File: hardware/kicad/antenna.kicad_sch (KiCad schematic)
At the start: 12 parts, among them U13 MM8130-2600, U14 MM8130-2600, U15 SKY13414-485LF, U16 SKY13414-485LF, U17 MM8130-2600, U18 MM8130-2600

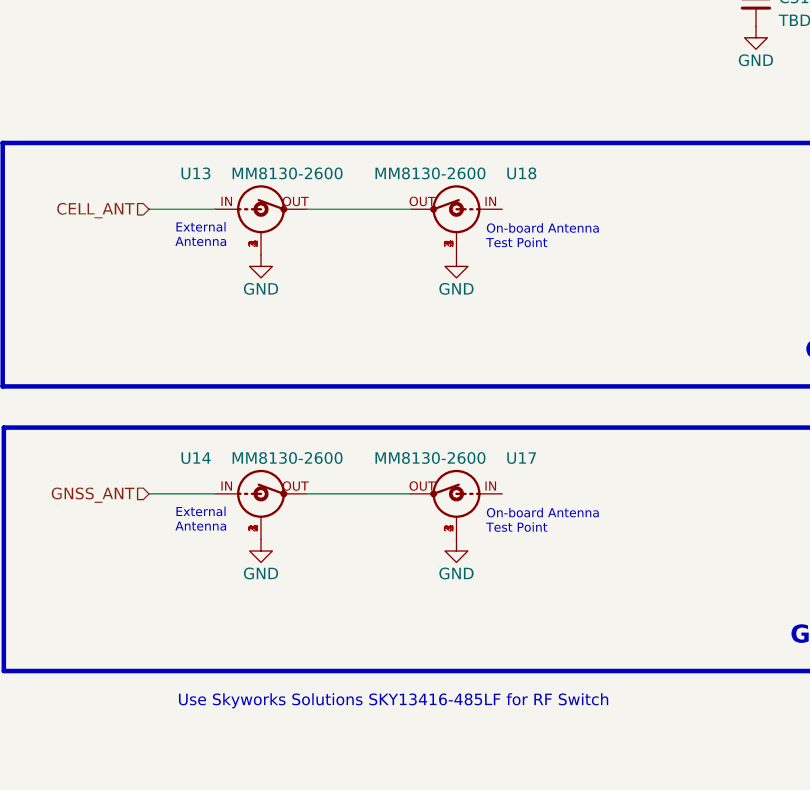
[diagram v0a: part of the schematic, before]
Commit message: remove antenna switch
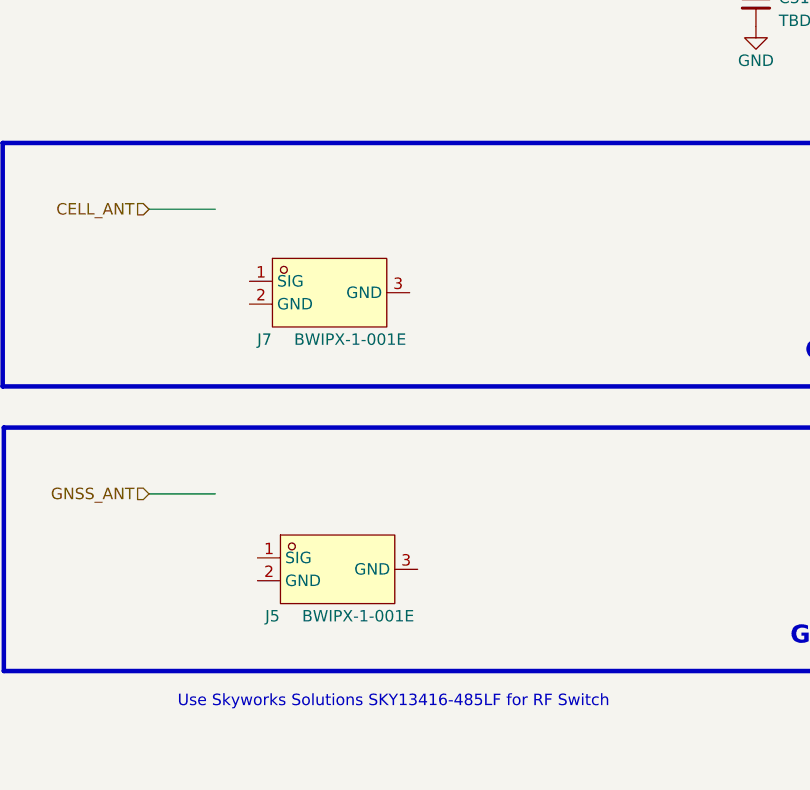
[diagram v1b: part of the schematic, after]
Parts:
- removed U13, U14, U17, U18: MM8130-2600, bwlc1a:MM8130-2600, symbol bwlc1a:MM8130-2600
- added J5, J7: BWIPX-1-001E, bwlc1a:BWIPX-1-001E, symbol bwlc1a:BWIPX-1-001E
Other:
- note removed: "External Antenna"
- note removed: "On-board Antenna Test Point"

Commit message: update antenna
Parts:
- added R20 (x2): 0, Resistor_SMD:R_0402_1005Metric, symbol Device:R_Small
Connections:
- net CELL_ANT: now also R20.1
- net GND: now also U15.15 (GND), U16.15 (GND)
- net at R20.1: now also U16.13 (ANT)
- net at J7.1 (SIG): now also R20.1, R20.2
- net at E1.1: now also R21.2
- net CELL_ANT_OUT: now reaches U15.13 (ANT)
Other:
- moved on the sheet: C31, C32, E1, J5, J7, R20, R21, U15, U16

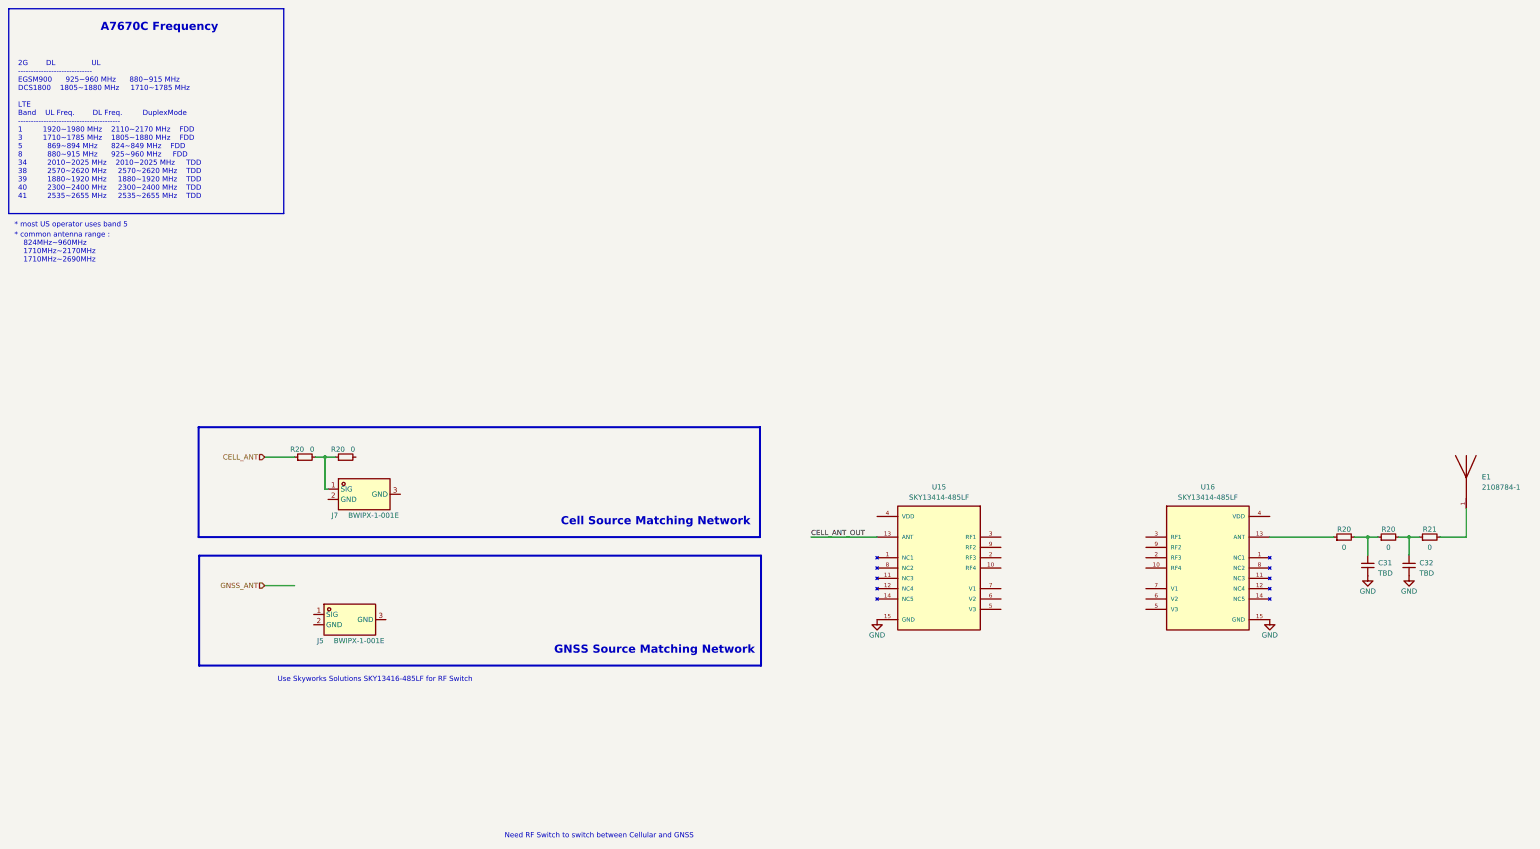
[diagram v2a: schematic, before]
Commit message: add te connectivity antenna schematicY
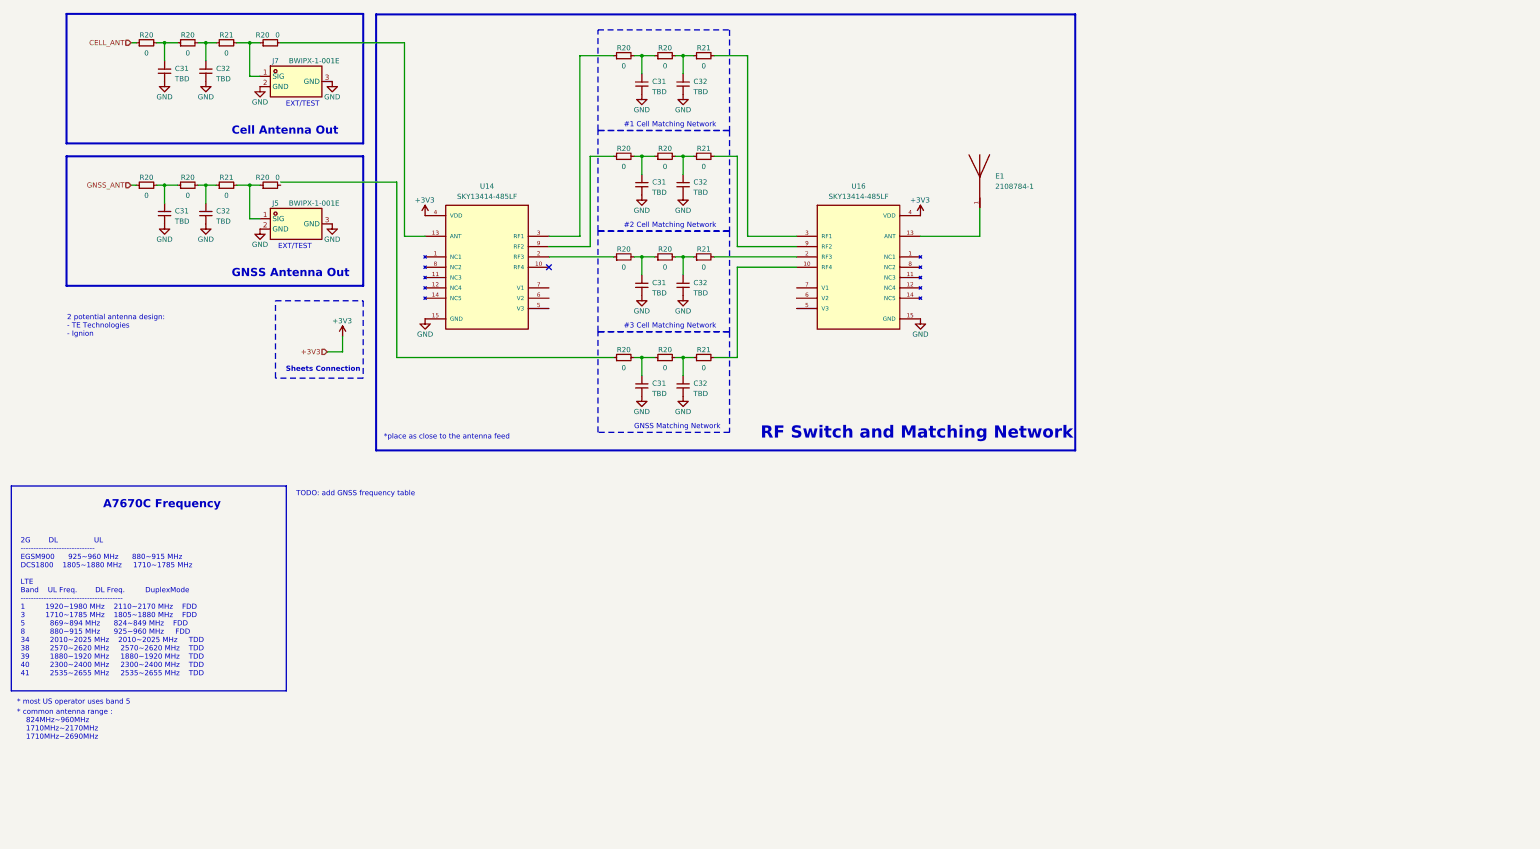
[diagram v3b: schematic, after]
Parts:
- removed C31, C32: TBD, Capacitor_SMD:C_0402_1005Metric, symbol Device:C_Small
- removed R20 (x4), R21: 0, Resistor_SMD:R_0402_1005Metric, symbol Device:R_Small
- removed U15: SKY13414-485LF, symbol bwlc1a:SKY13414-485LF
- added C31 (x6), C32 (x6): TBD, Capacitor_SMD:C_0402_1005Metric, symbol Device:C_Small
- added R20 (x14), R21 (x6): 0, Resistor_SMD:R_0402_1005Metric, symbol Device:R_Small
- added U14: SKY13414-485LF, symbol bwlc1a:SKY13414-485LF
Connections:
- net CELL_ANT: now also R20.1
- net GND: now also J5.2 (GND), J5.3 (GND), J7.2 (GND), J7.3 (GND), C31.2, C31.2, C31.2, C31.2, C31.2, C31.2, C32.2, C32.2, C32.2, C32.2, C32.2, C32.2, U14.15 (GND)
- net GNSS_ANT: now also R20.1
- net at U16.13 (ANT): now also E1.1
- net at J7.1 (SIG): now also R20.1, R21.2
- net at U16.10 (RF4): now also R21.2
- net at U16.2 (RF3): now also R21.2
- net at U16.3 (RF1): now also R21.2
- net +3V3: now reaches U16.4 (VDD)
- net +3V3: now also U14.4 (VDD)
- net at U16.9 (RF2): now also R21.2
- net at J5.1 (SIG): now also R20.1, R21.2
- new net: C32.1, R20.2, R21.1 (x6)
- new net: R20.2, U14.13 (ANT)
- new net: C31.1, R20.1, R20.2 (x6)
- new net: R20.1, U14.2 (RF3)
- new net: R20.1, U14.9 (RF2)
- new net: R20.1, U14.3 (RF1)
- no-connect marks 0 -> 1
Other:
- note added: "#1 Cell Matching Network"
- note added: "#2 Cell Matching Network"
- note added: "#3 Cell Matching Network"
- note added: "*place as close to the antenna feed"
- note added: "2 potential antenna design: - TE Technologies - Ignion"
- note added: "Cell Antenna Out"
- note added: "EXT/TEST"
- note added: "GNSS Antenna Out"
- note added: "GNSS Matching Network"
- note added: "RF Switch and Matching Network"
- note added: "Sheets Connection"
- note added: "TODO: add GNSS frequency table"
- note removed: "Cell Source Matching Network"
- note removed: "GNSS Source Matching Network"
- note removed: "Need RF Switch to switch between Cellular and GNSS"
- note removed: "Use Skyworks Solutions SKY13416-485LF for RF Switch"
- moved on the sheet: E1, U16

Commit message: add todo comment
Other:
- note added: "TODO: check design guide for rf switch"
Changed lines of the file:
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@@
+    (effects (font (size 1.27 1.27)) (justify left bottom))
+  )
+  (text "TODO: check design guide for rf switch" (at 114.3 53.975 0)
     (effects (font (size 1.27 1.27)) (justify left bottom))
   )

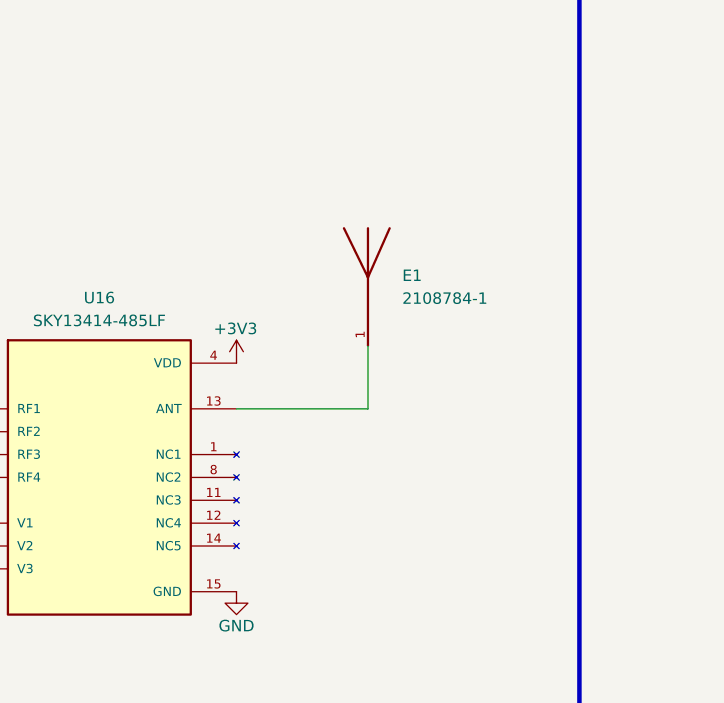
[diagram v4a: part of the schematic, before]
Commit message: add matching network close to antenna feed
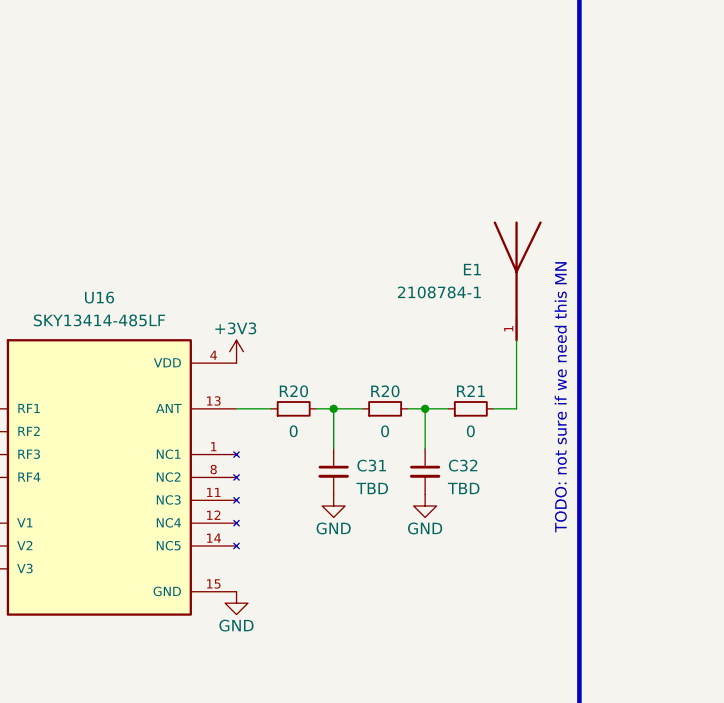
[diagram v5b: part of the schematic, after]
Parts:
- added C31, C32: TBD, Capacitor_SMD:C_0402_1005Metric, symbol Device:C_Small
- added R20 (x2), R21: 0, Resistor_SMD:R_0402_1005Metric, symbol Device:R_Small
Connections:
- net GND: now also C31.2, C32.2
- net at E1.1: now also R21.2; no longer U16.13 (ANT)
- new net: C31.1, R20.1, R20.2
- new net: C32.1, R20.2, R21.1
- new net: R20.1, U16.13 (ANT)
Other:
- note added: "TODO: not sure if we need this MN"
- moved on the sheet: E1

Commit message: clean-up
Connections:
- net at R20.2: now also R20.1

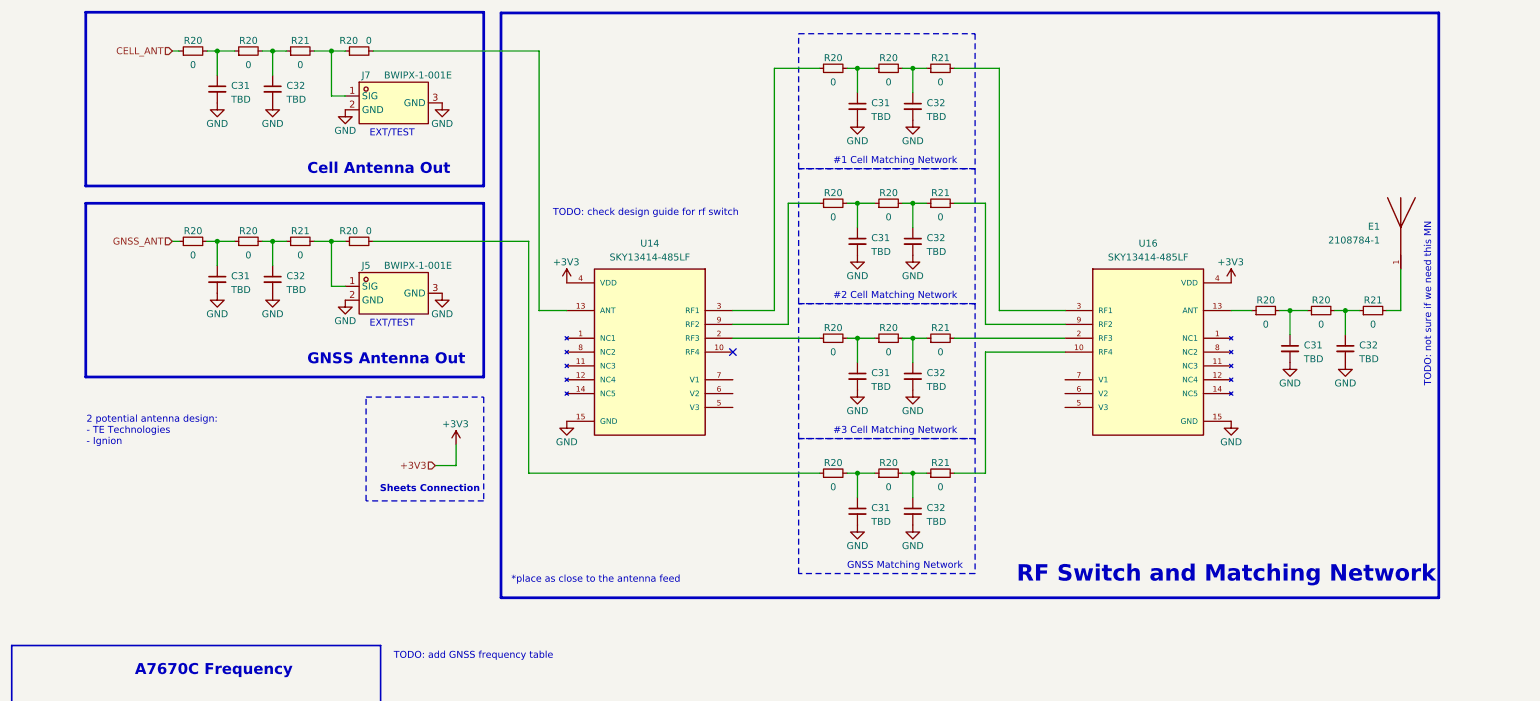
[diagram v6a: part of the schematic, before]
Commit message: clean-up and update antenna
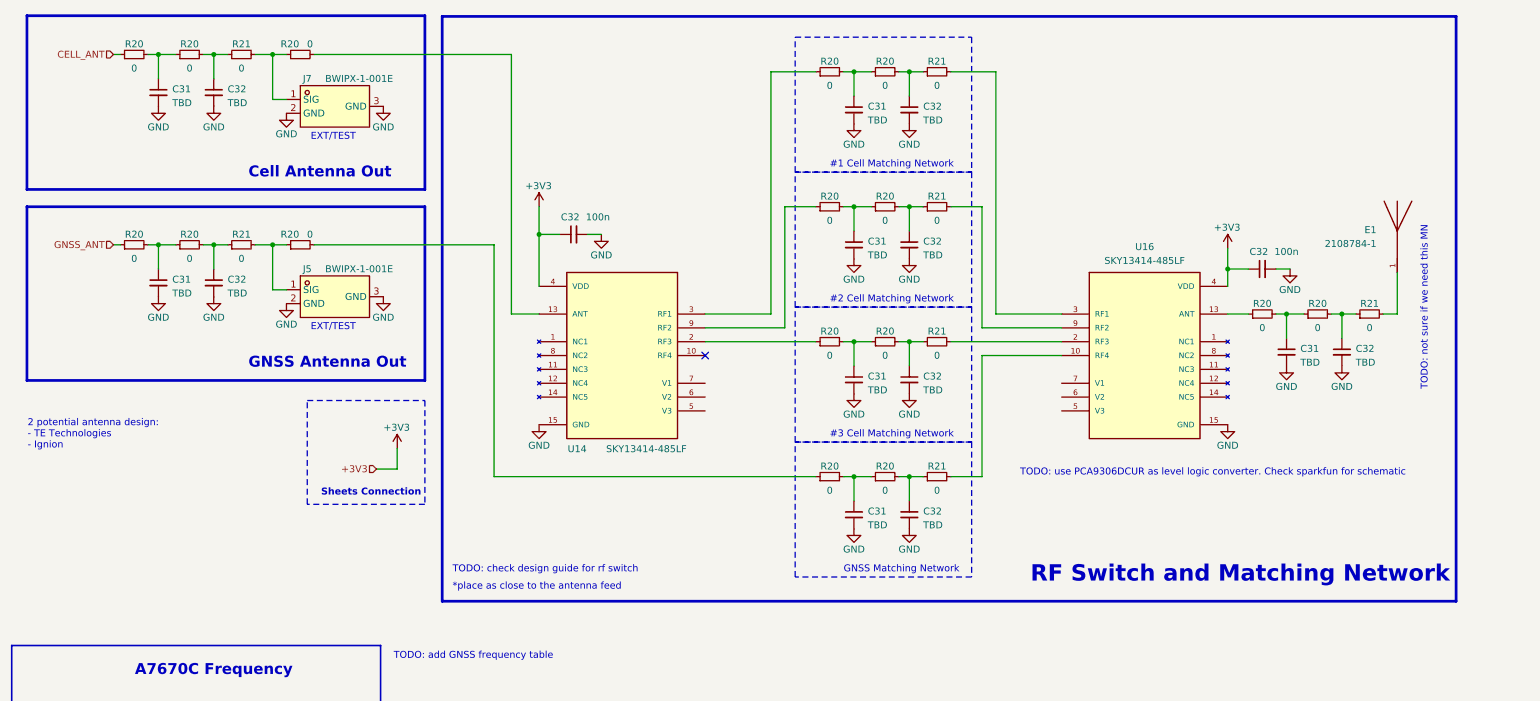
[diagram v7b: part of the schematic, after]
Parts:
- added C32 (x2): 100n, Capacitor_SMD:C_0402_1005Metric, symbol Device:C_Small
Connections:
- net +3V3: now also C32.1, C32.1
- net GND: now also C32.2, C32.2
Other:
- note added: "TODO: use PCA9306DCUR as level logic converter. Check sparkfun for schematic"
- moved on the sheet: C31, C32, E1, J5, J7, R20, R21, U14, U16

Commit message: ignion antenna design
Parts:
- removed C31 (x5), C32 (x5): TBD, Capacitor_SMD:C_0402_1005Metric, symbol Device:C_Small
- removed C32 (x2): 100n, Capacitor_SMD:C_0402_1005Metric, symbol Device:C_Small
- removed E1: 2108784-1, bwlc1a:2108784-1, symbol bwlc1a:2108784-1
- removed R20 (x10), R21 (x5): 0, Resistor_SMD:R_0402_1005Metric, symbol Device:R_Small
- removed U14, U16: SKY13414-485LF, symbol bwlc1a:SKY13414-485LF
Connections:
- no-connect marks 1 -> 0
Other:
- note added: "Antenna and Matching Network"
- note added: "TODO: - does cellular power cap have a specific ESR? - maybe change GNSS 2V8 with lower Iq https://www.lcsc.com/product-detail/Linear-Voltage-Regulators-LDO_Texas-Instruments-TPS7A0328DBVR_C2862669.html - look for lower LDO Iq for GNSS 3V3 - consider adding ESD in all schematic"
- note added: "TODO: change to use 2 ignion antenna. All rf switch sub-section most likely will need to be removed"
- note removed: "#1 Cell Matching Network"
- note removed: "#2 Cell Matching Network"
- note removed: "#3 Cell Matching Network"
- note removed: "GNSS Matching Network"
- note removed: "RF Switch and Matching Network"
- note removed: "TODO: check design guide for rf switch"
- note removed: "TODO: not sure if we need this MN"
- note removed: "TODO: use PCA9306DCUR as level logic converter. Check sparkfun for schematic"
